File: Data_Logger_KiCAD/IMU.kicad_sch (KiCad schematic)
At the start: 0 parts

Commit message: adding labels and updating IMU sch
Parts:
- added C16, C17: 100 nF, symbol Device:C
- added C18, C33, C34: 100n, Capacitor_SMD:C_0402_1005Metric, symbol Device:C_Small
- added C35: 1u, Capacitor_SMD:C_0402_1005Metric, symbol Device:C_Small
- added U1: LSM6DSO32TR, LSM6DSO32TR:XDCR_LSM6DSO32TR, symbol LSM6DSO32:LSM6DSO32TR
- added U3: ADXL375, custom:LGA_CC-14-1_ADI, symbol custom:ADXL375
- added U5: BMI088, custom:PQFN50P450X300X100-16N, symbol bmi088:BMI088
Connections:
- new net: U1.10 (NC), U1.11 (NC)
- new net +3V3: C16.1, C17.1, C18.1, C33.1, C34.1, C35.1, U1.5 (VDDIO), U1.8 (VDD), U3.1 (VDDIO), U3.6 (VS), U5.11 (VDDIO), U5.3 (VDD)
- new net ACCEL_INT: U5.16 (INT1)
- new net CS_IMU: U1.12 (CS)
- new net GND: C16.2, C17.2, C18.2, C33.2, C34.2, C35.2, U1.2 (SDX), U1.3 (SCX), U1.4 (INT1), U1.6 (GND), U1.7 (GND), U1.9 (INT2), U3.2 (GND), U3.4 (GND), U3.5 (GND), U5.2 (NC), U5.4 (GNDA), U5.6 (GNDIO), U5.7 (PS)
- new net HIGHG_INT: U3.8 (INT1)
- new net MISO: U3.12 (SDO/ALT), U5.10 (SDO2), U5.15 (SDO1)
- new net MOSI: U3.13 (SDA/SDI/SDIO), U5.9 (SDA/SDI)
- new net SCK: U3.14 (SCL/SCLK), U5.8 (SCL/SCK)
- new net SDI: U1.14 (SDA)
- new net SDO: U1.1 (SDO/SA0)
- new net SPC: U1.13 (SCL)
- new net ~{ACCEL_CS}: U5.14 (CSB1)
- new net ~{GYRO_CS}: U5.5 (CSB2)
- new net ~{HIGHG_CS}: U3.7 (~{CS})
- no-connect marks 0 -> 4
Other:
- note added: "(pins and connections are identical for both IMUs). INT1 and INT2 Default: output forced to ground. Double check whether or not we will need them."
- note added: "ISM6HG256X"
- note added: "Pretend this symbol is an ISM6HG256X"

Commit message: add CS's
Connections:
- net SDI is gone; now on net MOSI: U1.14 (SDA)
- net SDO is gone; now on net MISO: U1.1 (SDO/SA0)
- net SPC is gone; now on net SCK: U1.13 (SCL)
- net CS_IMU renamed IMU_CS
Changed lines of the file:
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@@
 		)
 	)
-	(hierarchical_label "CS_IMU"
+	(hierarchical_label "IMU_CS"
 		(shape input)
 		(at 88.9 59.69 0)
@@
 		)
 	)
-	(hierarchical_label "SPC"
+	(hierarchical_label "SCK"
 		(shape input)
 		(at 91.44 52.07 0)
@@
 		)
 	)
-	(hierarchical_label "SDO"
+	(hierarchical_label "MISO"
 		(shape output)
 		(at 99.06 57.15 0)
@@
 		)
 	)
-	(hierarchical_label "SDI"
+	(hierarchical_label "MOSI"
 		(shape input)
 		(at 91.44 54.61 0)

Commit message: rem old files and add LCSC #'s
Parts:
- C16, C17: footprint (none) -> Capacitor_SMD:C_0402_1005Metric; LCSC (none) -> C1525
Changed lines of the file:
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@@
 			)
 		)
-		(property "Footprint" ""
+		(property "Footprint" "Capacitor_SMD:C_0402_1005Metric"
 			(at 131.7752 57.15 0)
 			(effects
@@
 			)
 		)
+		(property "LCSC" "C1525"
+			(at 130.81 53.34 0)
+			(effects
+				(font
+					(size 1.27 1.27)
+				)
+				(hide yes)
+			)
+		)
 		(pin "2"
 		)
@@
 			)
 		)
-		(property "Footprint" ""
+		(property "Footprint" "Capacitor_SMD:C_0402_1005Metric"
 			(at 117.8052 57.15 0)
 			(effects
@@
 			(at 116.84 53.34 0)
 			(effects
+				(font
+					(size 1.27 1.27)
+				)
+				(hide yes)
+			)
+		)
+		(property "LCSC" "C1525"
+			(at 116.84 53.34 0)
+			(effects

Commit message: partial MCU layout
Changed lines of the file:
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@@
 					(size 1.27 1.27)
 				)
-				(hide yes)
 			)
 		)

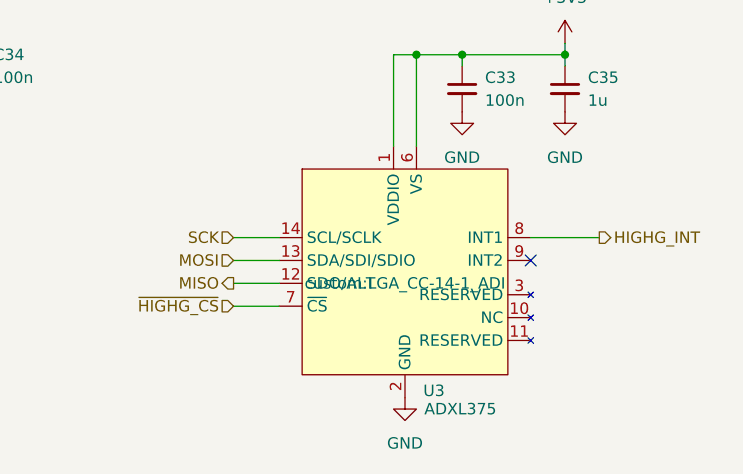
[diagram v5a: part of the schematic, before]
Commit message: fix footprint errors
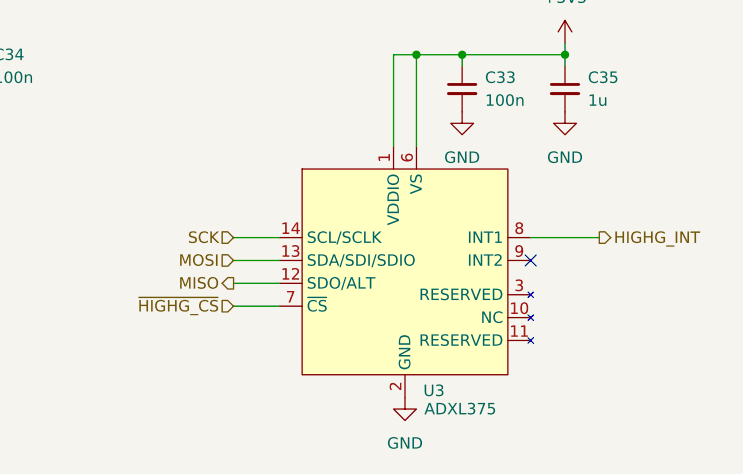
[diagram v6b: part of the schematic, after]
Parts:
- U1: footprint LSM6DSO32TR:XDCR_LSM6DSO32TR -> custom:XDCR_LSM6DSO32TR
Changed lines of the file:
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@@
 					(size 1.27 1.27)
 				)
+				(hide yes)
 			)
 		)
@@
 			)
 		)
-		(property "Footprint" "LSM6DSO32TR:XDCR_LSM6DSO32TR"
+		(property "Footprint" "custom:XDCR_LSM6DSO32TR"
 			(at 66.04 52.07 0)
 			(effects

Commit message: footprint + sd tweaks
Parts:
- U1: footprint custom:XDCR_LSM6DSO32TR -> Package_LGA:LGA-14_3x2.5mm_P0.5mm_LayoutBorder3x4y
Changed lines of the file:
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@@
 			)
 		)
-		(property "Footprint" "custom:XDCR_LSM6DSO32TR"
+		(property "Footprint" "Package_LGA:LGA-14_3x2.5mm_P0.5mm_LayoutBorder3x4y"
 			(at 66.04 52.07 0)
 			(effects
